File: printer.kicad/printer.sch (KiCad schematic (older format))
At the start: 34 parts, among them J1 ZX_Spectrum_128K_expansion, J2 Conn_01x06_Male, J3 Conn_01x05_Male, J4 Conn_01x04_Male, U1 SN74AHC373, U2 SN74HCT00, U3 SN74AHCT02, U4 SN74AHC373, U5 XC6206PxxxMR, U6 STM32F103C8Tx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

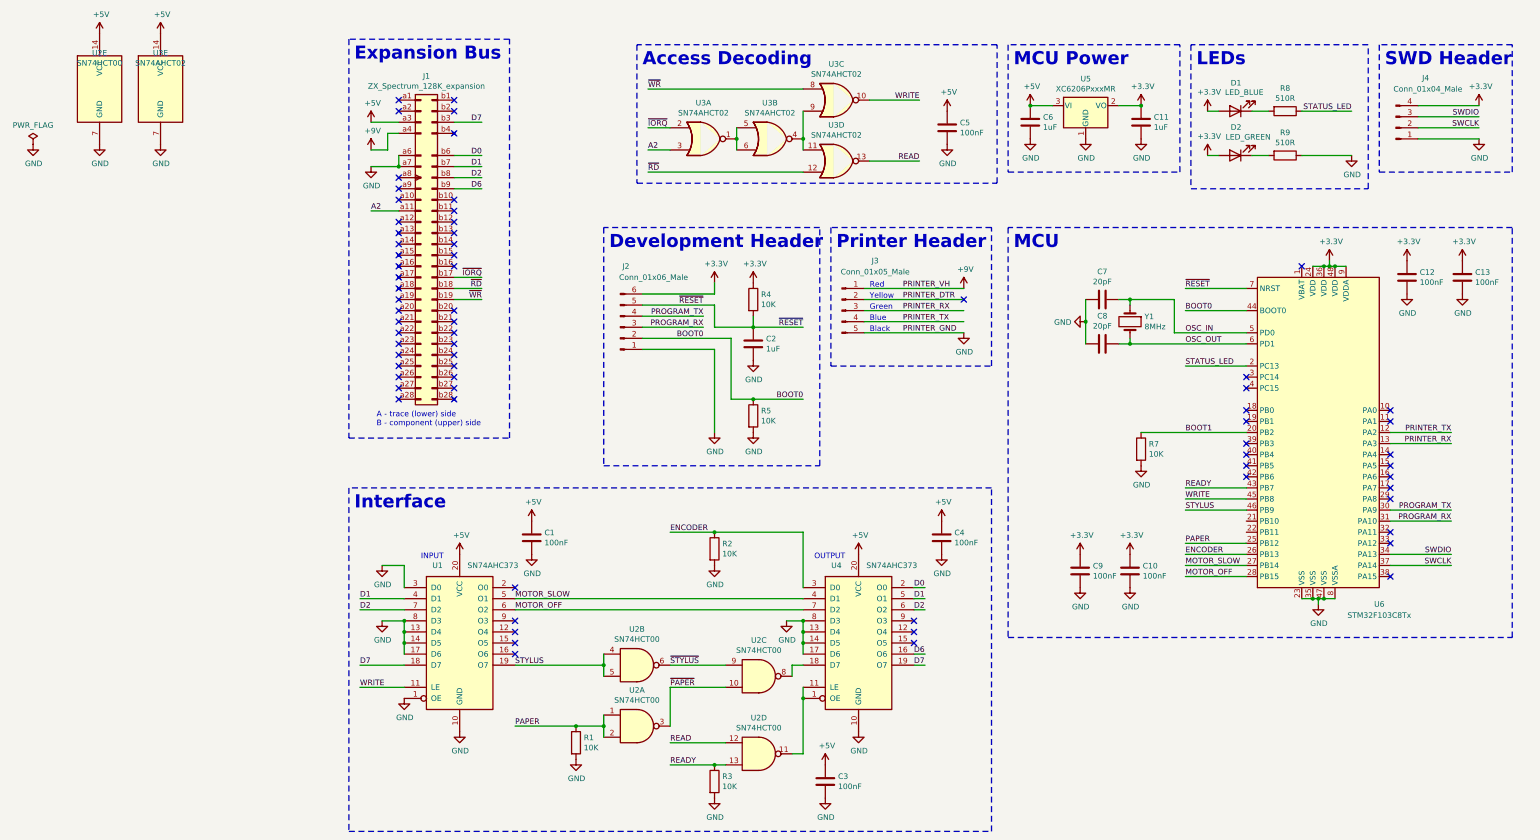
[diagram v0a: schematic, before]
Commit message: Switch to parts in stock at LCSC
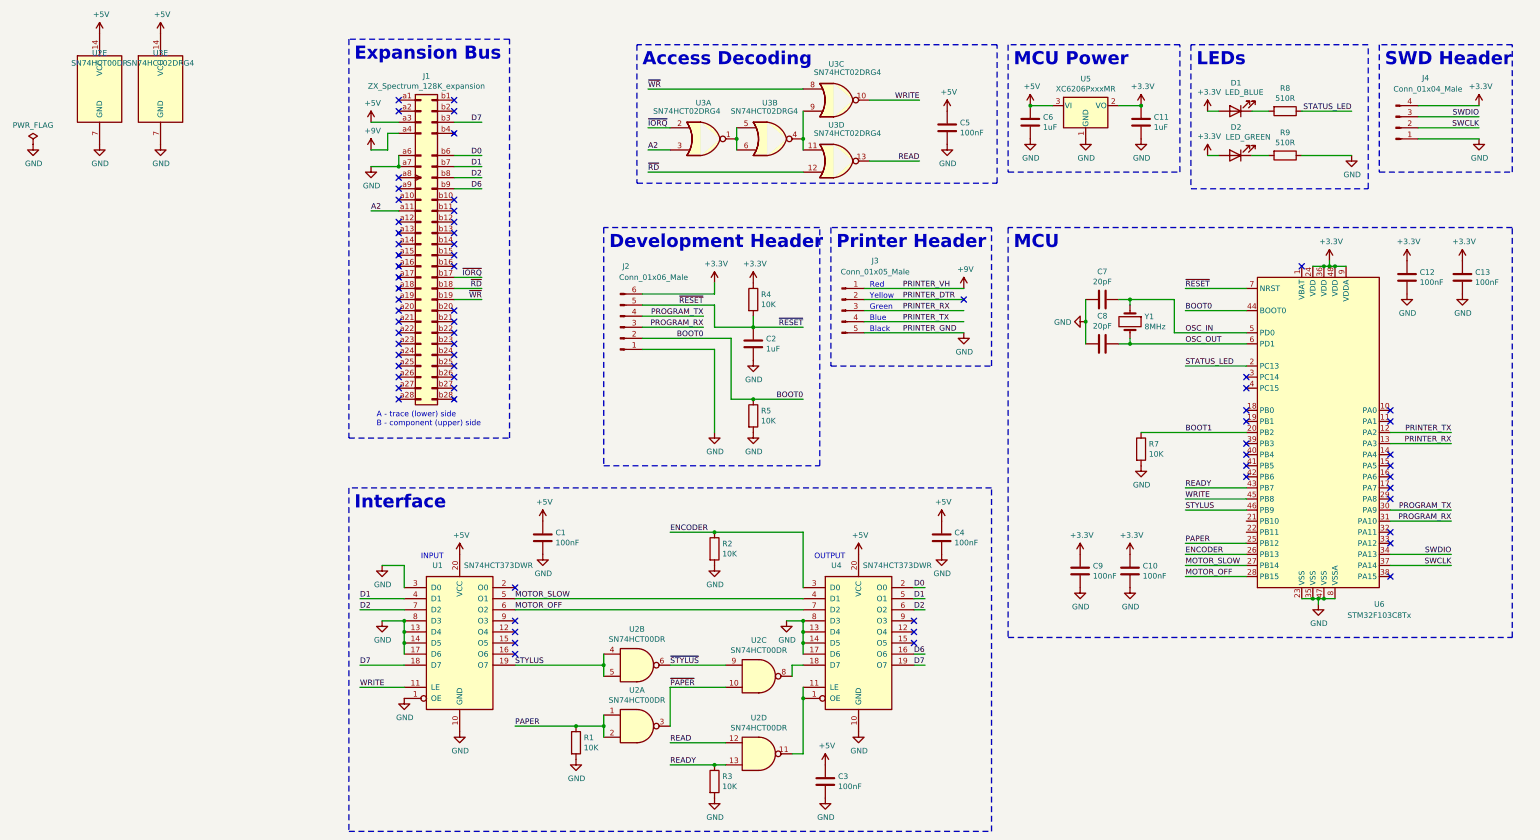
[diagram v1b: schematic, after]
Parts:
- C1, C10, C12, C13, C3, C4, C5, C9: LCSC C14663 -> C24452
- U1, U4: value SN74AHC373 -> SN74HCT373DWR; footprint Package_SO:TSSOP-20_4.4x6.5mm_P0.65mm -> Package_SO:SOIC-20W_7.5x12.8mm_P1.27mm; LCSC C80242 -> C132265
- U2: value SN74HCT00 -> SN74HCT00DR; footprint Package_SO:TSSOP-14_4.4x5mm_P0.65mm -> Package_SO:SOIC-14_3.9x8.7mm_P1.27mm; LCSC C131694 -> C6764
- U3: value SN74AHCT02 -> SN74HCT02DRG4; footprint Package_SO:TSSOP-14_4.4x5mm_P0.65mm -> Package_SO:SOIC-14_3.9x8.7mm_P1.27mm; LCSC C87964 -> C6765
- Y1: LCSC C115962 -> C156253
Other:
- moved on the sheet: C1

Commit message: Label OUTPUT net
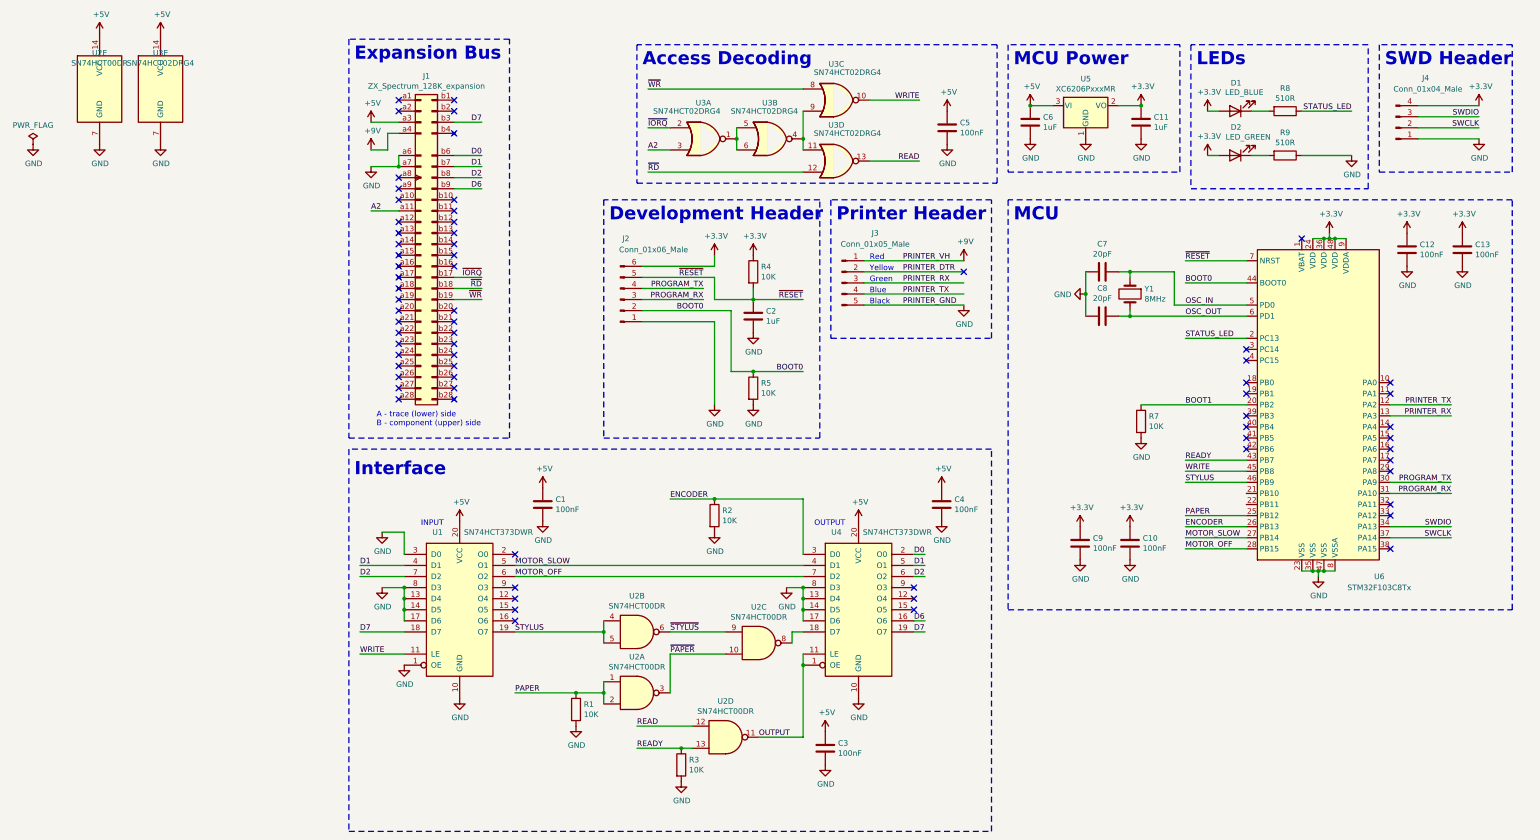
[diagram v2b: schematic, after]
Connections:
- net labels added: OUTPUT
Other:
- moved on the sheet: C1, C10, C12, C13, C2, C3, C4, C7, C8, C9, J2, J3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

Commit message: schematics: Add printer current sensing
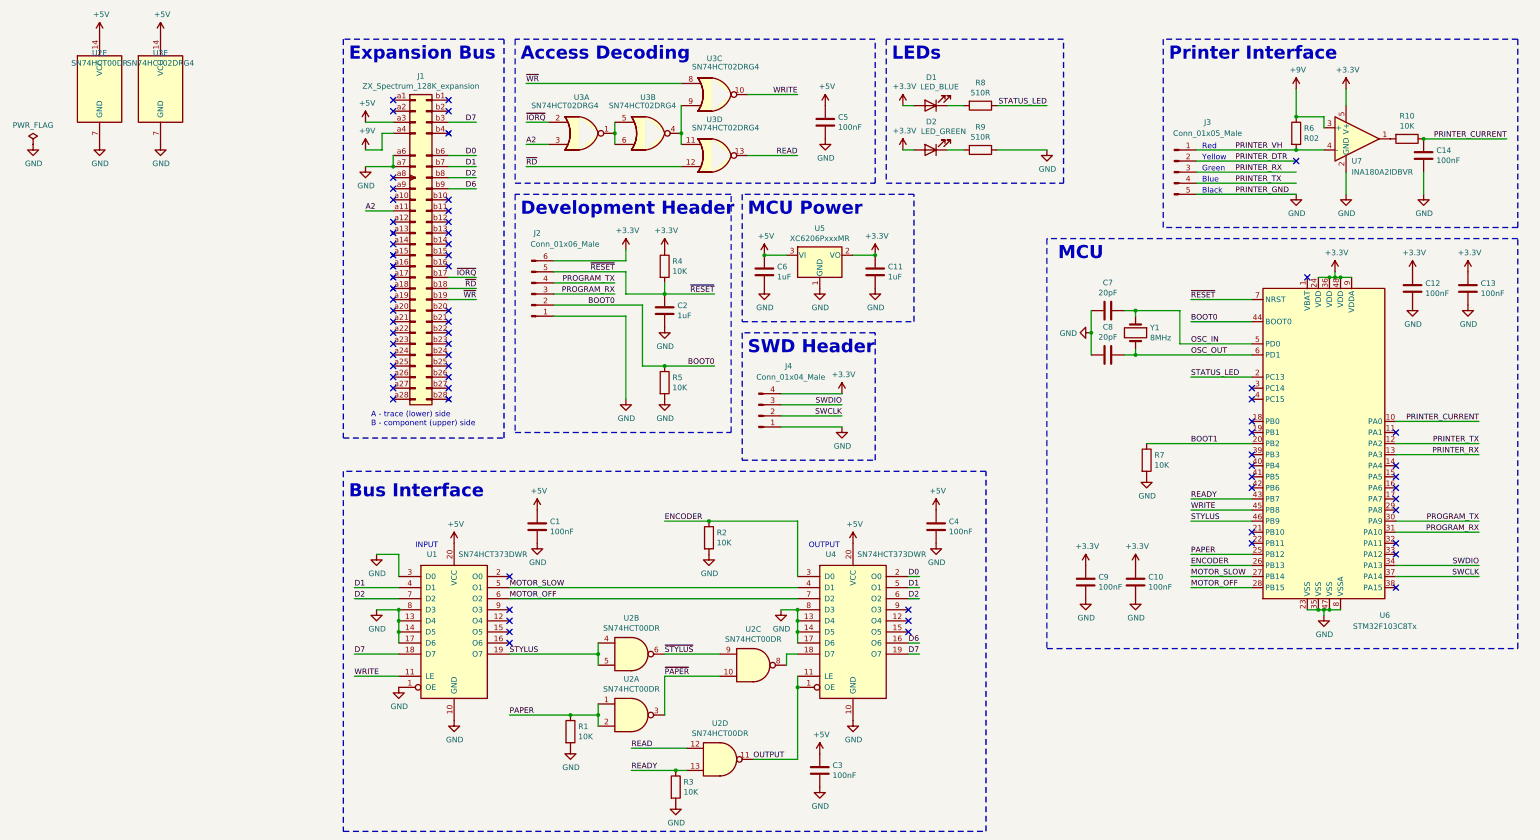
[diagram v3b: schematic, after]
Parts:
- added C14: 100nF, Capacitor_SMD:C_0603_1608Metric, symbol Device:C
- added R10: 10K, Resistor_SMD:R_0603_1608Metric, symbol Device:R
- added R6: R02, Resistor_SMD:R_1206_3216Metric, symbol Device:R
- added U7: INA180A2IDBVR, Package_TO_SOT_SMD:SOT-23-5, symbol printer:INA180A2
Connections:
- net labels added: PRINTER_CURRENT
- wire segments 136 -> 145
- no-connect marks 69 -> 70
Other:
- note added: "Bus Interface"
- note added: "Printer Interface"
- note removed: "Interface"
- note removed: "Printer Header"
- moved on the sheet: C1, C10, C11, C12, C13, C2, C3, C4, C5, C6, C7, C8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

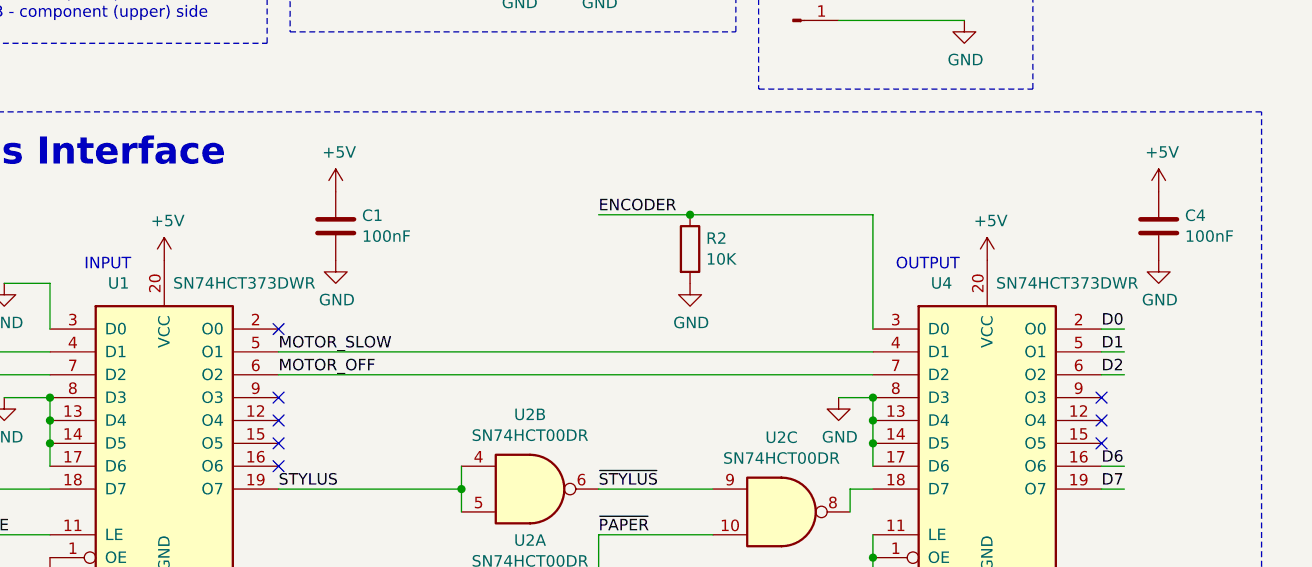
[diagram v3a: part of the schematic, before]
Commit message: Switch to in-stock LCSC latches
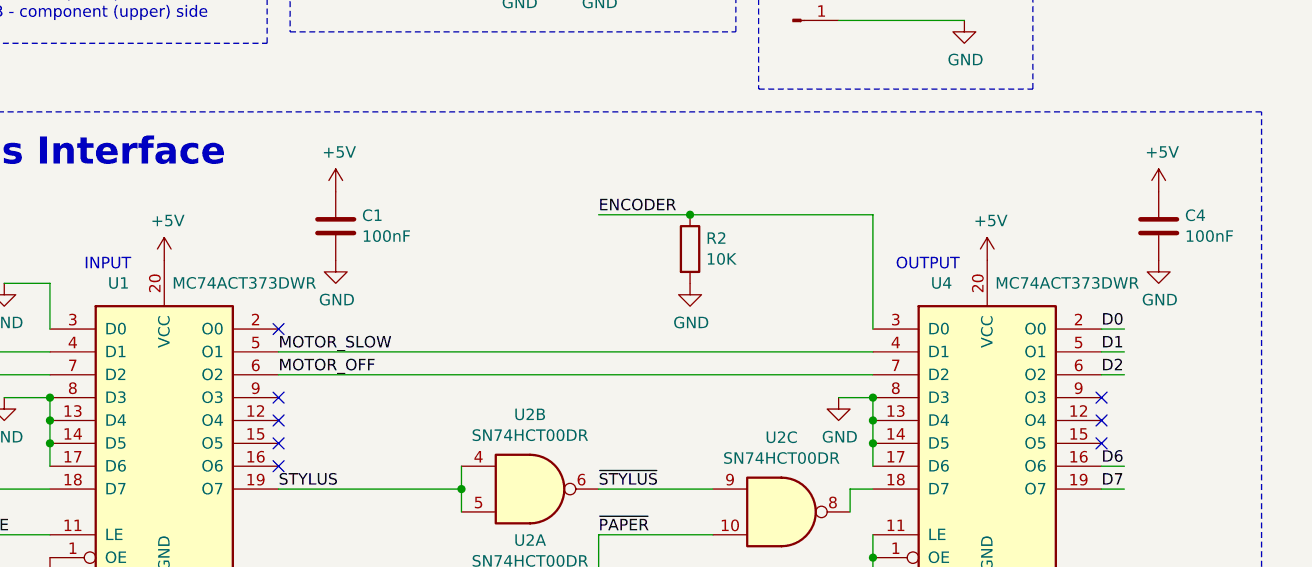
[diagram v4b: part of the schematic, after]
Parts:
- U1, U4: value SN74HCT373DWR -> MC74ACT373DWR; LCSC C132265 -> C233456
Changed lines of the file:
@@
 P 5150 5900
 F 0 "U4" H 4950 6600 50  0000 C CNN
-F 1 "SN74HCT373DWR" H 5500 6600 50  0000 C CNN
+F 1 "MC74ACT373DWR" H 5500 6600 50  0000 C CNN
 F 2 "Package_SO:SOIC-20W_7.5x12.8mm_P1.27mm" H 5150 5900 50  0001 C CNN
-F 3 "https://datasheet.lcsc.com/szlcsc/1806052129_Texas-Instruments-SN74HCT373DWR_C132265.pdf" H 5150 5900 50  0001 C CNN
-F 4 "C132265" H 5150 5900 50  0001 C CNN "LCSC"
+F 3 "https://datasheet.lcsc.com/szlcsc/ON-Semicon-ON-MC74ACT373DWR2G_C233456.pdf" H 5150 5900 50  0001 C CNN
+F 4 "C233456" H 5150 5900 50  0001 C CNN "LCSC"
 	1    5150 5900
 	1    0    0    -1
@@
 P 1550 5900
 F 0 "U1" H 1350 6600 50  0000 C CNN
-F 1 "SN74HCT373DWR" H 1900 6600 50  0000 C CNN
+F 1 "MC74ACT373DWR" H 1900 6600 50  0000 C CNN
 F 2 "Package_SO:SOIC-20W_7.5x12.8mm_P1.27mm" H 1550 5900 50  0001 C CNN
-F 3 "https://datasheet.lcsc.com/szlcsc/1806052129_Texas-Instruments-SN74HCT373DWR_C132265.pdf" H 1550 5900 50  0001 C CNN
-F 4 "C132265" H 1550 5900 50  0001 C CNN "LCSC"
+F 3 "https://datasheet.lcsc.com/szlcsc/ON-Semicon-ON-MC74ACT373DWR2G_C233456.pdf" H 1550 5900 50  0001 C CNN
+F 4 "C233456" H 1550 5900 50  0001 C CNN "LCSC"
 	1    1550 5900
 	1    0    0    -1
@@
 NoConn ~ 8750 5100
 $Comp
-L power:+3.3V #PWR?
+L power:+3.3V #PWR0105
 U 1 1 5F0E74DB
 P 9600 1000
-F 0 "#PWR?" H 9600 850 50  0001 C CNN
+F 0 "#PWR0105" H 9600 850 50  0001 C CNN
 F 1 "+3.3V" H 9615 1173 50  0000 C CNN
 F 2 "" H 9600 1000 50  0001 C CNN

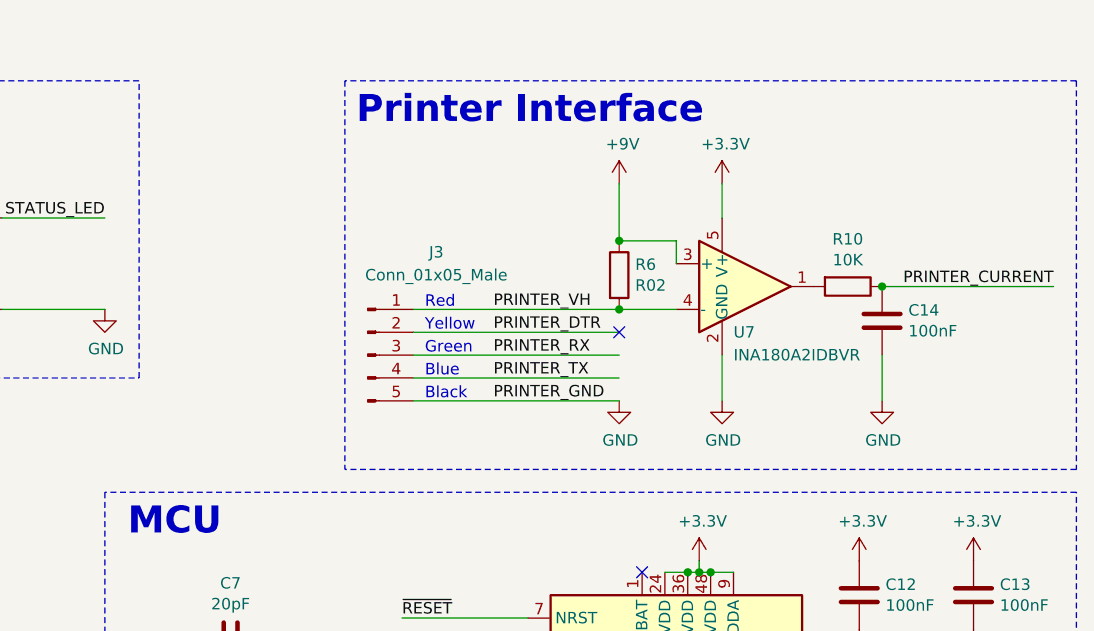
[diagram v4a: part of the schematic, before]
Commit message: Add bypass cap for current sense amp
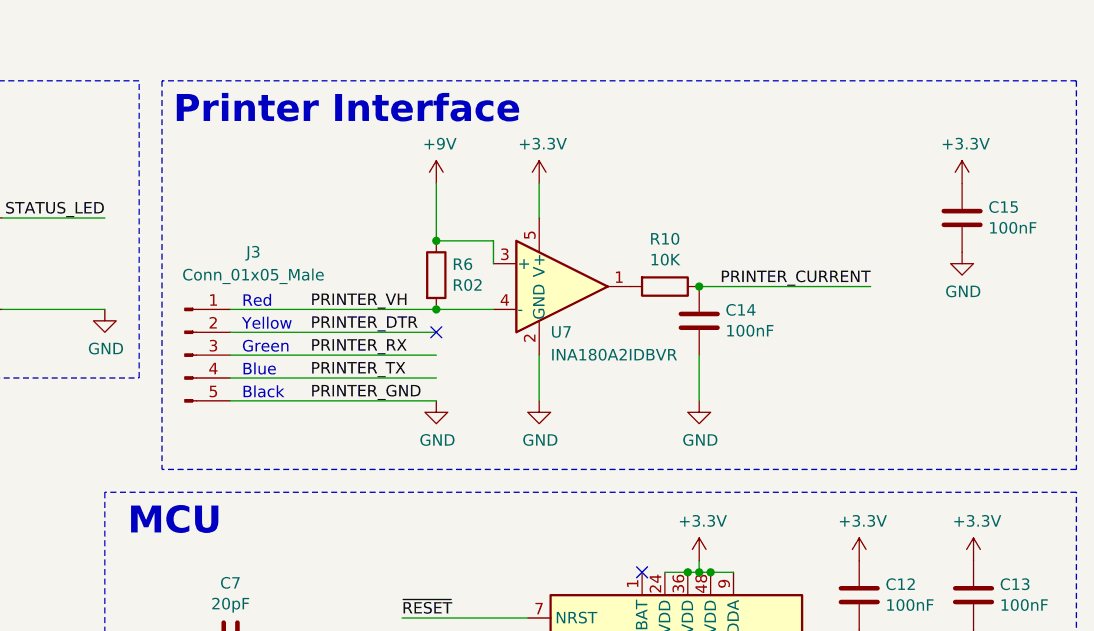
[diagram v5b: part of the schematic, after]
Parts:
- added C15: 100nF, Capacitor_SMD:C_0603_1608Metric, symbol Device:C
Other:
- moved on the sheet: C14, J3, R10, R6, U7
